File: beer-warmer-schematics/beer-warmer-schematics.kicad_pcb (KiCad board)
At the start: 4 copper layers, 60 x 42.8 mm, 41 parts, among them J1 USB_C_Receptacle_USB2.0_14P, J2 Screw_Terminal_01x02, J3 Conn_01x07_Socket, J4 Conn_01x07_Socket, J5 Conn_01x04_Pin, J6 Screw_Terminal_01x03, Q1 AOD4184A, U2 LM2596S-5, U3 CH224K, U4 INA219AxDCN

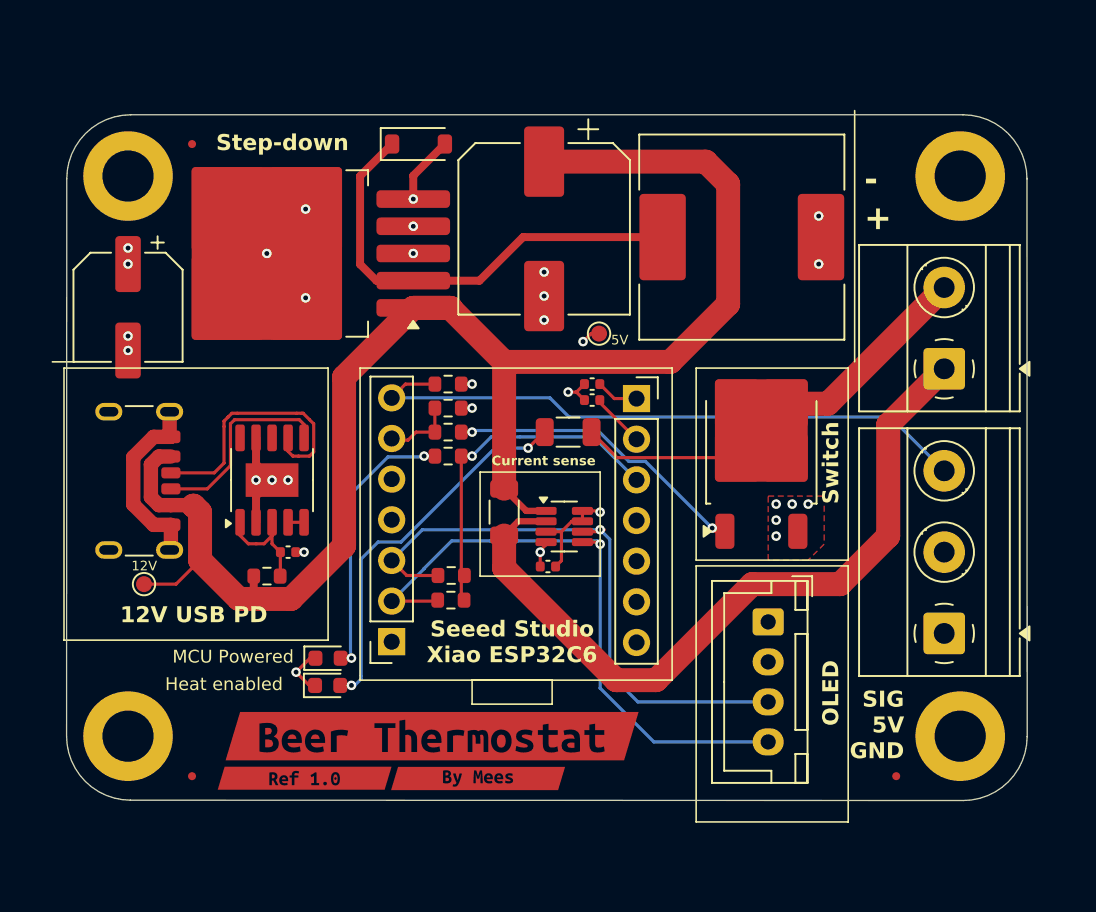
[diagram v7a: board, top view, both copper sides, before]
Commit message: slightly better decoupling cap placement
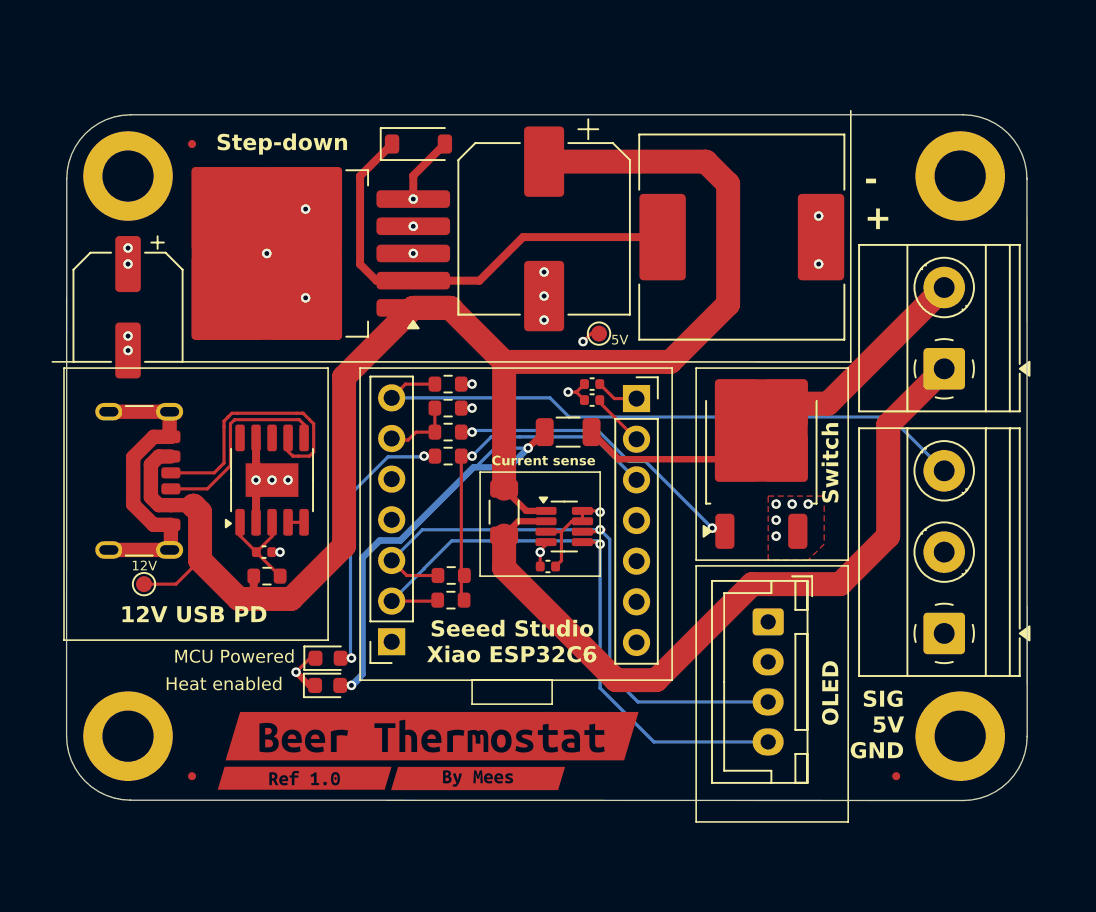
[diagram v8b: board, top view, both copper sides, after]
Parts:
- moved C6 1.50 mm to (132.0, 98.5)
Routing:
- net Net-(D2-A): track 24.0 -> 45.4 mm
- net HEAT-: track 22.8 -> 32.5 mm
- net GND: track 35.2 -> 42.8 mm
- net VDD: track 7.67 -> 6.69 mm
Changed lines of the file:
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@@
 	(footprint "Capacitor_SMD:C_0402_1005Metric"
 		(layer "F.Cu")
-		(at 133.5 98.5 180)
+		(at 132 98.5 180)
 		(descr "Capacitor SMD 0402 (1005 Metric), square (rectangular) end terminal, IPC_7351 nominal, (Body size source: IPC-SM-782 page 76, https://www.pcb-3d.com/wordpress/wp-content/uploads/ipc-sm-782a_amendment_1_and_2.pdf), generated with kicad-footprint-generator")
 		(tags "capacitor")
@@
 	)
 	(gr_line
+		(start 126.91 86.61)
+		(end 168.662213 86.618525)
+		(stroke
+			(width 0.1)
+			(type default)
+		)
+		(layer "F.SilkS")
+	)
+	(gr_line
 		(start 120.09 86.61)
 		(end 118.765612 86.61)
@@
 	)
 	(gr_line
-		(start 168.903562 86.61)
-		(end 168.904479 70.907363)
+		(start 168.662213 86.618525)
+		(end 168.66313 70.915888)
 		(stroke
 			(width 0.1)
@@
 	)
 	(gr_text "MCU Powered"
-		(at 133.863293 105.5 0)
+		(at 133.943126 105.501944 0)
 		(layer "F.SilkS")
 		(effects
@@
 	)
 	(segment
-		(start 132.5 97.474999)
-		(end 132.5 96.6375)
-		(width 0.2)
-		(layer "F.Cu")
-		(net 1)
-	)
-	(segment
-		(start 133.02 98.5)
-		(end 133.02 99.985)
-		(width 0.2)
-		(layer "F.Cu")
-		(net 1)
-	)
-	(segment
-		(start 132.5 97.98)
-		(end 133.02 98.5)
+		(start 130.5 97.48)
+		(end 131.52 98.5)
 		(width 0.2)
 		(layer "F.Cu")
@@
 	)
 	(segment
-		(start 131.02 97.98)
-		(end 130.5 97.46)
-		(width 0.2)
-		(layer "F.Cu")
-		(net 1)
-	)
-	(segment
-		(start 131.994999 97.98)
-		(end 132.5 97.474999)
+		(start 131.52 98.515)
+		(end 133.005 100)
 		(width 0.2)
 		(layer "F.Cu")
@@
 	)
 	(segment
-		(start 131.5 97.98)
-		(end 131.02 97.98)
+		(start 132.5 96.6375)
+		(end 132.5 97.52)
 		(width 0.2)
 		(layer "F.Cu")
@@
 	)
 	(segment
-		(start 130.5 97.46)
-		(end 130.5 96.6375)
+		(start 130.5 96.6375)
+		(end 130.5 97.48)
 		(width 0.2)
 		(layer "F.Cu")
@@
 	)
 	(segment
-		(start 131.5 97.98)
-		(end 131.994999 97.98)
+		(start 131.52 98.5)
+		(end 131.52 98.515)
 		(width 0.2)
 		(layer "F.Cu")
@@
 	)
 	(segment
-		(start 132.5 96.6375)
-		(end 132.5 97.98)
+		(start 132.5 97.52)
+		(end 131.52 98.5)
 		(width 0.2)
 		(layer "F.Cu")
@@
 	)
 	(segment
-		(start 149.5375 91)
-		(end 149.5 91)
-		(width 0.4)
+		(start 136.931971 107)
+		(end 136.761665 106.829694)
+		(width 0.2)
 		(layer "F.Cu")
 		(net 4)
 	)
 	(segment
-		(start 149.5 91)
-		(end 148.5 92)
-		(width 0.2)
+		(start 149.5375 91)
+		(end 149.5 91)
+		(width 0.4)
 		(layer "F.Cu")
 		(net 4)
 	)
 	(segment
-		(start 136.761665 106.829694)
-		(end 137.456833 106.829694)
-		(width 0.2)
+		(start 137.456833 106.829694)
+		(end 137.460788 106.825739)
+		(width 0.4)
 		(layer "F.Cu")
 		(net 4)
 	)
 	(segment
-		(start 136.931971 107)
-		(end 136.761665 106.829694)
-		(width 0.2)
+		(start 149.5 91)
+		(end 148.5 92)
+		(width 0.4)
 		(layer "F.Cu")
 		(net 4)
 	)
 	(segment
-		(start 137.456833 106.829694)
-		(end 137.460788 106.825739)
-		(width 0.2)
+		(start 136.761665 106.829694)
+		(end 137.456833 106.829694)
+		(width 0.4)
 		(layer "F.Cu")
 		(net 4)
@@
 	)
 	(segment
+		(start 148.5 92)
+		(end 147.299 93.201)
+		(width 0.4)
+		(layer "B.Cu")
+		(net 4)
+	)
+	(segment
+		(start 138.160531 98.839469)
+		(end 138.160531 106.125996)
+		(width 0.4)
+		(layer "B.Cu")
+		(net 4)
+	)
+	(segment
+		(start 138.160531 106.125996)
+		(end 137.460788 106.825739)
+		(width 0.4)
+		(layer "B.Cu")
+		(net 4)
+	)
+	(segment
 		(start 138.060531 98.939469)
 		(end 138.060531 106.221217)
@@
 	)
 	(segment
+		(start 139.231 97.769)
+		(end 138.160531 98.839469)
+		(width 0.4)
+		(layer "B.Cu")
+		(net 4)
+	)
+	(segment
+		(start 147.299 93.201)
+		(end 145.08548 93.201)
+		(width 0.4)
+		(layer "B.Cu")
+		(net 4)
+	)
+	(segment
 		(start 148.5 92)
 		(end 146.4279 92)
@@
 	)
 	(segment
+		(start 145.08548 93.201)
+		(end 140.51748 97.769)
+		(width 0.4)
+		(layer "B.Cu")
+		(net 4)
+	)
+	(segment
 		(start 138.060531 106.439469)
 		(end 137.5 107)
@@
 	)
 	(segment
+		(start 140.51748 97.769)
+		(end 139.231 97.769)
+		(width 0.4)
+		(layer "B.Cu")
+		(net 4)
+	)
+	(segment
 		(start 139.131 97.869)
 		(end 138.060531 98.939469)
@@
 	)
 	(segment
-		(start 134.829694 106.829694)
-		(end 134 106)
-		(width 0.2)
-		(layer "F.Cu")
-		(net 22)
-	)
-	(segment
 		(start 151 88.5)
 		(end 151.52 88.5)
@@
 	)
 	(segment
-		(start 133.98 98.5)
-		(end 134.5 98.5)
+		(start 132.48 98.5)
+		(end 133 98.5)
 		(width 0.2)
 		(layer "F.Cu")
@@
 	)
 	(segment
+		(start 122.298973 98.365995)
+		(end 126.098973 98.365995)
+		(width 0.9)
+		(layer "F.Cu")
+		(net 22)
+	)
+	(segment
 		(start 126.098973 89.725995)
 		(end 126.098973 91.215995)
@@
 		(start 135.186665 106.829694)
 		(end 134.829694 106.829694)
-		(width 0.2)
+		(width 0.4)
 		(layer "F.Cu")
 		(net 22)
@@
 	)
 	(segment
+		(start 132.5 98.48)
+		(end 132.52 98.5)
+		(width 0.2)
+		(layer "F.Cu")
+		(net 22)
+	)
+	(segment
 		(start 123.826973 92.567956)
 		(end 123.826973 95.524035)
@@
 	)
 	(segment
+		(start 122.298973 89.725995)
+		(end 126.098973 89.725995)
+		(width 0.9)
+		(layer "F.Cu")
+		(net 22)
+	)
+	(segment
+		(start 134.829694 106.829694)
+		(end 134 106)
+		(width 0.4)
+		(layer "F.Cu")
+		(net 22)
+	)
+	(segment
 		(start 151.89497 95.924003)
 		(end 152.924003 95.924003)
@@
 	)
 	(via
-		(at 134.5 98.5)
+		(at 133 98.5)
 		(size 0.6)
 		(drill 0.3)
@@
 	)
 	(segment
+		(start 161.426162 92.696338)
+		(end 154.158838 92.696338)
+		(width 0.4)
+		(layer "F.Cu")
+		(net 24)
+	)
+	(segment
 		(start 161.5475 92.575)
 		(end 161.526162 92.596338)
@@
 		(layer "F.Cu")
 		(net 24)
+	)
+	(segment
+		(start 154.158838 92.696338)
+		(end 152.4625 91)
+		(width 0.4)
+		(layer "F.Cu")
+		(net 24)
